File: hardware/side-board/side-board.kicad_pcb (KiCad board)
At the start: 4 copper layers, 294 parts, among them IC101 TPS62933DRLR, IC102 NUP2105LT1G, IC201 STM32C092KCT6, IC202 TCAN332DR, IC203 TPS56A37RPAR, IC204 INA181A1IDBVR, IC301 STM32C092KCT6, IC302 TCAN332DR, IC303 TPS56A37RPAR, IC304 INA181A1IDBVR, IC401 STM32C092KCT6, IC402 TCAN332DR, IC403 TPS56A37RPAR, IC404 INA181A1IDBVR, J101 Inter-board Connector, J102 Inter-board Connector, J103 XT30 VBAT, J201 Servo Connector, J202 Servo Connector, J203 Servo Connector, J204 TC2050, J205 Conn_01x06, J301 Servo Connector, J302 Servo Connector, J303 Servo Connector, J304 TC2050, J305 Conn_01x06, J401 Servo Connector, J402 Servo Connector, J403 Servo Connector, J404 TC2050, J405 Conn_01x06, Y201 Crystal_GND24, Y301 Crystal_GND24, Y401 Crystal_GND24

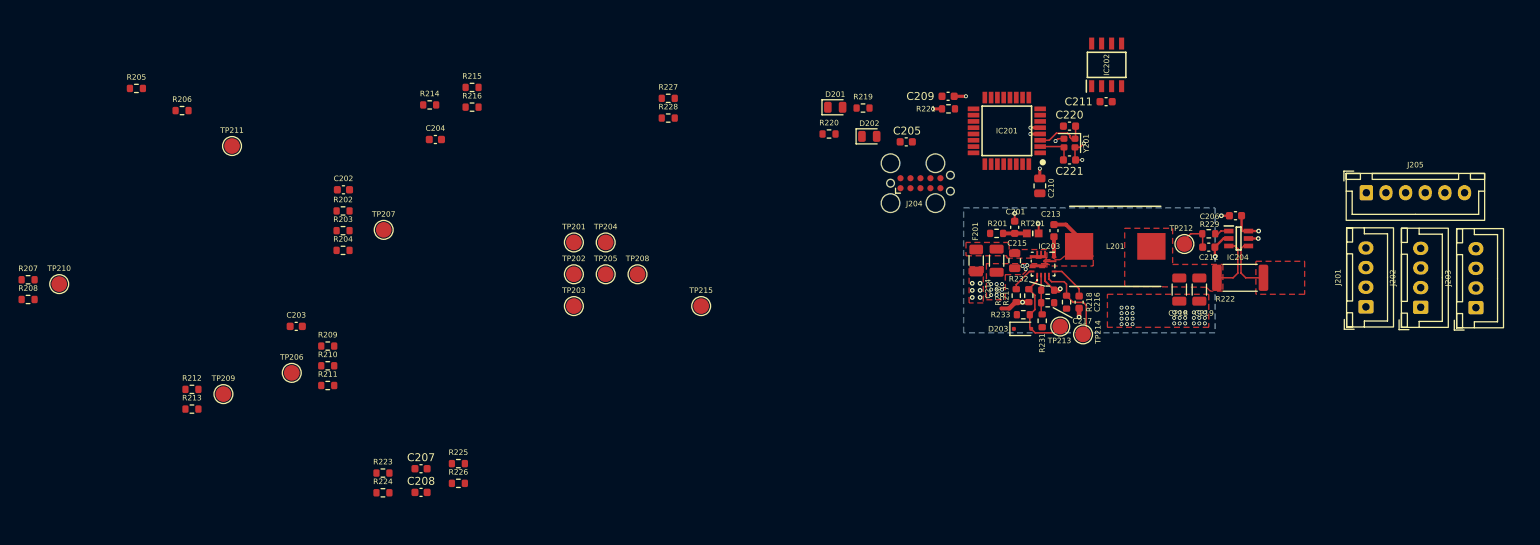
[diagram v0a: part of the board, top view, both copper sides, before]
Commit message: Updated PCB placement side-board
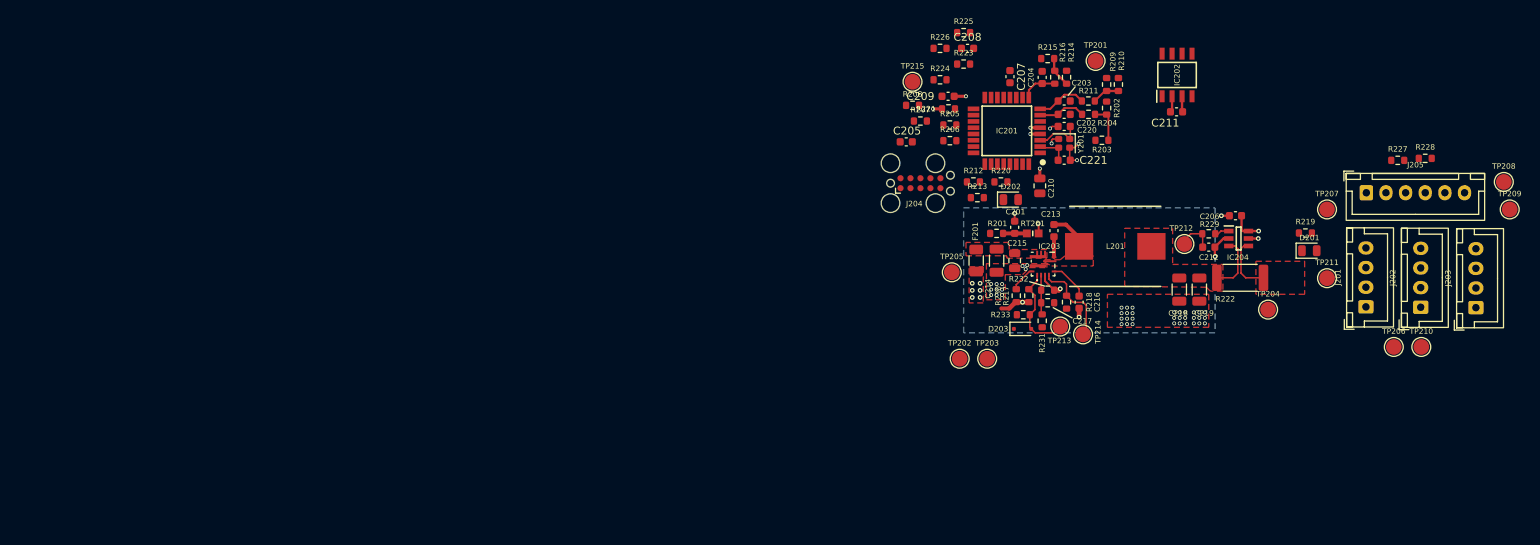
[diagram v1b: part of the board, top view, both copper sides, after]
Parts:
- moved TP210 173.5 mm to (214.8, 54.5)
- moved TP209 165.4 mm to (226.0, 37.0)
- moved TP211 140.4 mm to (202.8, 45.8)
- moved TP206 140.3 mm to (211.2, 54.5)
- moved TP207 120.1 mm to (202.8, 37.0)
- moved R207 115.3 mm to (151.0, 25.8)
- moved R208 115.2 mm to (150.0, 23.8)
- moved TP208 110.9 mm to (225.2, 33.5)
- moved R210 106.8 mm to (176.2, 21.1), turned to -90 degrees
- moved R209 104.6 mm to (174.7, 21.1), turned to -90 degrees
- moved R205 103.6 mm to (154.8, 26.2)
- moved R213 103.5 mm to (158.2, 35.5)
- moved R211 103.4 mm to (172.4, 23.2), turned to 180 degrees
- moved R212 102.9 mm to (157.8, 33.5)
- moved C203 101.9 mm to (169.3, 23.2)
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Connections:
- C216 pad 2: AGND -> /Leg_A/AGND
- C316 pad 2: AGND -> /Leg_B/AGND
- C416 pad 2: AGND -> /Leg_C/AGND
- IC203 pad 3: AGND -> /Leg_A/AGND
- IC303 pad 3: AGND -> /Leg_B/AGND
- IC403 pad 3: AGND -> /Leg_C/AGND
- NT201 pad 1: AGND -> /Leg_A/AGND
- NT301 pad 1: AGND -> /Leg_B/AGND
- NT401 pad 1: AGND -> /Leg_C/AGND
- R217 pad 1: AGND -> /Leg_A/AGND
- R230 pad 1: AGND -> /Leg_A/AGND
- R232 pad 2: AGND -> /Leg_A/AGND
- R317 pad 1: AGND -> /Leg_B/AGND
- R330 pad 1: AGND -> /Leg_B/AGND
- R332 pad 2: AGND -> /Leg_B/AGND
- R417 pad 1: AGND -> /Leg_C/AGND
- R430 pad 1: AGND -> /Leg_C/AGND
- R432 pad 2: AGND -> /Leg_C/AGND
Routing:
- net AGND: track 7.20 -> 0.00 mm, vias 3 -> 0
- net /Leg_A/AGND: track 0.00 -> 7.20 mm, vias 0 -> 3
- net /Leg_A/ADC_POT_FEMUR: track 0.00 -> 6.39 mm
- net /Leg_A/ADC_POT_COXA: track 0.00 -> 6.04 mm
- net Net-(R202-Pad2): track 0.00 -> 4.85 mm
- net /Leg_A/ADC_POT_TIBIA: track 0.00 -> 4.61 mm
- net Net-(R214-Pad2): track 0.00 -> 3.85 mm
- net Net-(R209-Pad2): track 0.00 -> 3.53 mm
- net GND: track 14.2 -> 17.6 mm, vias 51 -> 52
- net +3V3: track 9.23 -> 11.2 mm
- net /Leg_A/OSC_OUT: track 6.87 -> 6.04 mm
- net /Leg_A/OSC_IN: track 4.71 -> 4.20 mm
- added copper zone on In1.Cu, net /Leg_A/AGND
- removed copper zone on In1.Cu, net AGND

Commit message: Updated sideboard PCB
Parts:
- C101, C103, C104, C105: footprint Capacitor_SMD:C_0805_2012Metric -> Capacitor_SMD:C_0603_1608Metric
- H101, H102, H103, H104: footprint MountingHole:MountingHole_3.2mm_M3 -> MountingHole:MountingHole_3.2mm_M3_DIN965_Pad_TopBottom
- J103: footprint Connector_AMASS:AMASS_XT30PW-M_1x02_P2.50mm_Horizontal -> Connector_AMASS:AMASS_XT30U-M_1x02_P5.0mm_Vertical
- JP108: moved to B.Cu
- L101: footprint vector:INDPM116102X400N -> vector:INDPM4441X200N
- L201, L301, L401: footprint vector:INDPM116102X400N -> side-board:INDPM7973X540N
- R101, R102: footprint Resistor_SMD:R_0805_2012Metric -> Resistor_SMD:R_0603_1608Metric
- moved NT401 73.1 mm to (114.9, 181.8), turned to 180 degrees
- moved JP108 57.7 mm to (30.6, 119.7)
- moved J303 57.4 mm to (206.6, 122.7), turned to 90 degrees
- moved J403 57.4 mm to (174.8, 181.7), turned to 90 degrees
- moved NT301 57.3 mm to (146.7, 122.8), turned to 180 degrees
- moved C308 57.1 mm to (141.9, 89.7)
- moved C408 57.1 mm to (110.1, 148.7)
- moved C309 56.9 mm to (139.4, 95.8)
- moved C409 56.9 mm to (107.6, 154.8)
- moved J301 54.0 mm to (192.6, 122.5), turned to 90 degrees
- moved J401 54.0 mm to (160.8, 181.6), turned to 90 degrees
- moved J302 53.1 mm to (199.5, 122.6), turned to 90 degrees
- moved J402 53.1 mm to (167.8, 181.6), turned to 90 degrees
- moved C405 52.4 mm to (102.3, 160.6), turned to 180 degrees
- moved C305 52.4 mm to (134.1, 101.5), turned to 180 degrees
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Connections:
- net Net-(IC101-SW) renamed /SW
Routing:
- net GND: track 17.6 -> 52.9 mm, vias 52 -> 156
- net +3V3: track 11.2 -> 33.7 mm, vias 5 -> 15
- net /Leg_B/BUCK_EN: track 0.00 -> 12.2 mm
- net /Leg_C/BUCK_EN: track 0.00 -> 12.2 mm
- net /Leg_C/BUCK_PG: track 0.00 -> 11.4 mm
- net /Leg_B/BUCK_PG: track 0.00 -> 11.4 mm
- net /Leg_B/6V0_BUCK: track 0.00 -> 7.31 mm
- net /Leg_C/6V0_BUCK: track 0.00 -> 7.31 mm
- net /Leg_B/6V0: track 0.00 -> 7.31 mm
- net /Leg_C/6V0: track 0.00 -> 7.31 mm
- net /Leg_C/AGND: track 0.00 -> 7.20 mm, vias 0 -> 3
- net /Leg_B/AGND: track 0.00 -> 7.20 mm, vias 0 -> 3
- net /Leg_B/ADC_POT_FEMUR: track 0.00 -> 6.39 mm
- net /Leg_C/ADC_POT_FEMUR: track 0.00 -> 6.39 mm
- net /Leg_B/ADC_POT_COXA: track 0.00 -> 6.04 mm
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- added copper zone on F.Cu, net /Leg_B/6V0
- added copper zone on F.Cu, net /Leg_B/6V0_BUCK
- added copper zone on In1.Cu, net /Leg_B/AGND
- added copper zone on F.Cu, net /Leg_B/SW
- added copper zone on F.Cu, net /Leg_B/VBAT_F
- added copper zone on F.Cu, net /Leg_C/6V0
- added copper zone on F.Cu, net /Leg_C/6V0_BUCK
- added copper zone on In1.Cu, net /Leg_C/AGND
- added copper zone on F.Cu, net /Leg_C/SW
- added copper zone on F.Cu, net /Leg_C/VBAT_F
- added copper zone on F.Cu, net /SW

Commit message: Updated PCB placement sideboard
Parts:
- JP107: value Jumper_Open -> SIDE_BIT
- R203, R210, R215: moved to B.Cu
- moved C106 70.5 mm to (89.4, 89.5), turned to 0 degrees
- moved J101 66.6 mm to (85.0, 140.0)
- moved D101 60.7 mm to (88.7, 73.4)
- moved TP101 54.3 mm to (69.0, 135.5)
- moved TP102 51.7 mm to (75.8, 135.4)
- moved J102 47.9 mm to (71.5, 140.0)
- moved TP105 43.3 mm to (101.0, 82.2)
- moved IC102 36.0 mm to (72.5, 135.2), turned to 90 degrees
- moved TP104 35.4 mm to (42.8, 124.5), turned to -90 degrees
- moved C205 24.8 mm to (173.9, 26.4)
- moved D102 23.4 mm to (33.8, 116.6), turned to 90 degrees
- moved R104 23.1 mm to (69.1, 133.2), turned to 180 degrees
- moved TP103 22.4 mm to (80.4, 79.2)
- moved J103 21.1 mm to (86.3, 81.4)
- moved JP107 19.6 mm to (56.9, 104.4)
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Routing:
- net /Leg_A/ADC_POT_FEMUR: track 6.39 -> 0.00 mm
- net /Leg_A/ADC_POT_COXA: track 6.04 -> 0.00 mm
- net Net-(R202-Pad2): track 4.85 -> 0.00 mm
- net /CAN_L: track 0.00 -> 4.08 mm
- net Net-(R214-Pad2): track 3.85 -> 0.00 mm
- net /CAN_H: track 0.00 -> 3.80 mm
- net Net-(R209-Pad2): track 3.53 -> 0.00 mm
- net GND: track 52.9 -> 56.3 mm
- net /VBAT: track 0.00 -> 3.01 mm
- net /Leg_A/ADC_POT_TIBIA: track 4.61 -> 1.69 mm
- net /Leg_A/6V0_ADC: track 0.00 -> 2.66 mm
- net +3V3: track 33.7 -> 36.2 mm, vias 15 -> 13
- net /Leg_A/VBAT_ADC: track 0.00 -> 2.43 mm
- net /SW: track 4.00 -> 3.44 mm
- added copper zone on F.Cu, net +3V3

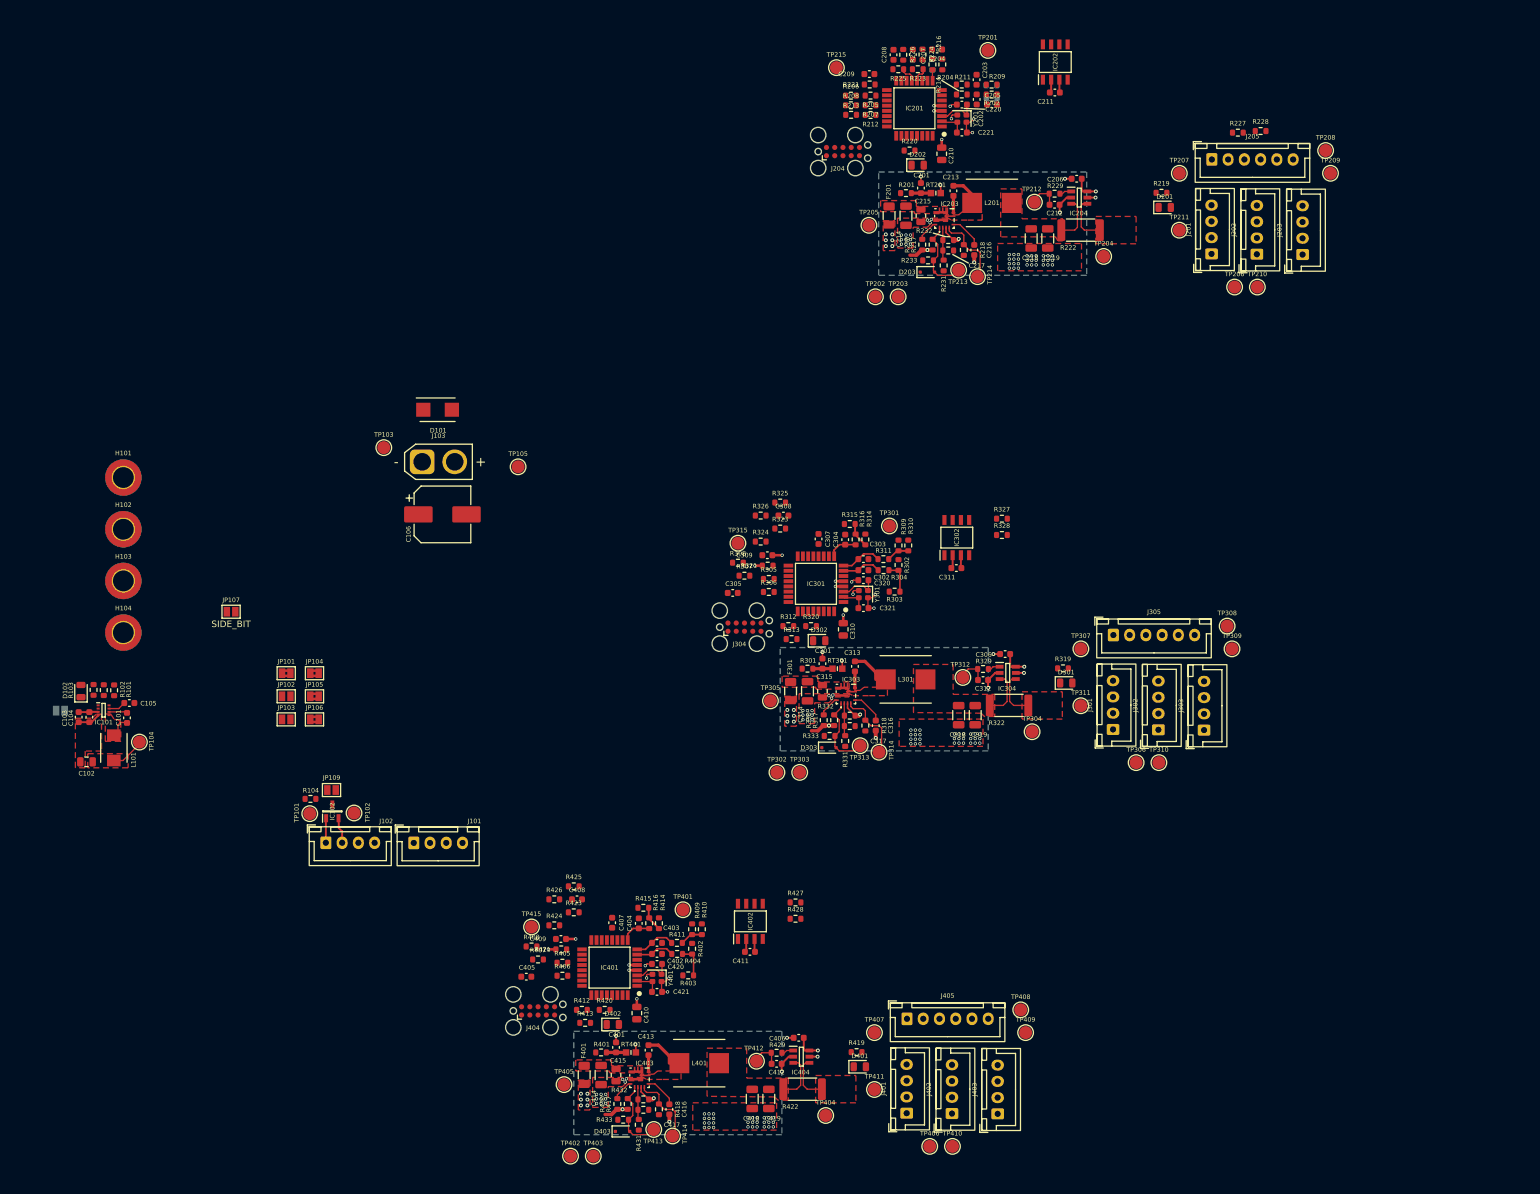
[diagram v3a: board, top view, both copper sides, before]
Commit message: Compacted side board pcb
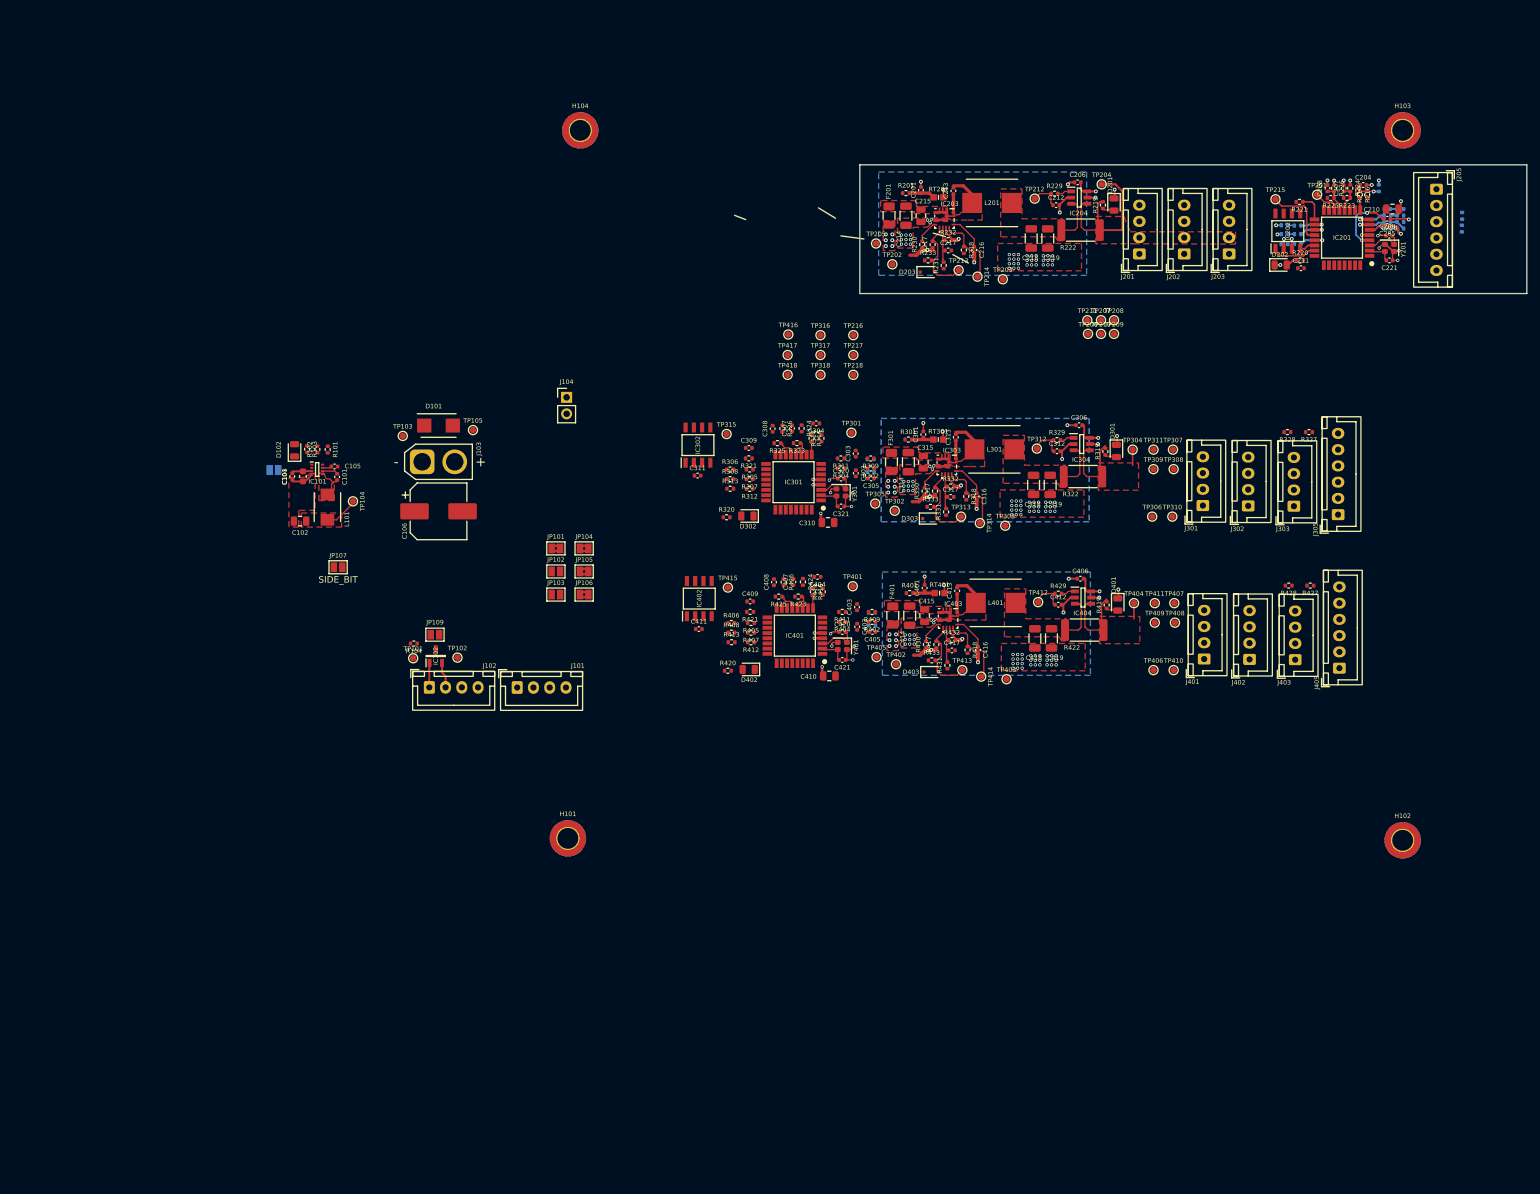
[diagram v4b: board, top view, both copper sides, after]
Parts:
- removed J204, J304, J404: TC2050, Connector:Tag-Connect_TC2050-IDC-FP_2x05_P1.27mm_Vertical
- added J104: SWD PWR, Connector_PinHeader_2.54mm:PinHeader_1x02_P2.54mm_Vertical, F.Cu at (108.5, 71.5)
- added TP216: SWDIO, TestPoint:TestPoint_Pad_D1.0mm, F.Cu at (152.6, 61.9)
- added TP217: SWCLK, TestPoint:TestPoint_Pad_D1.0mm, F.Cu at (152.6, 65.0)
- added TP218: NRST, TestPoint:TestPoint_Pad_D1.0mm, F.Cu at (152.6, 68.0)
- added TP316: SWDIO, TestPoint:TestPoint_Pad_D1.0mm, F.Cu at (147.6, 61.9)
- added TP317: SWCLK, TestPoint:TestPoint_Pad_D1.0mm, F.Cu at (147.6, 65.0)
- added TP318: NRST, TestPoint:TestPoint_Pad_D1.0mm, F.Cu at (147.6, 68.0)
- added TP416: SWDIO, TestPoint:TestPoint_Pad_D1.0mm, F.Cu at (142.6, 61.8)
- added TP417: SWCLK, TestPoint:TestPoint_Pad_D1.0mm, F.Cu at (142.5, 65.0)
- added TP418: NRST, TestPoint:TestPoint_Pad_D1.0mm, F.Cu at (142.5, 68.0)
- C101, C105, C201, C204, C205, C206, C207, C208, C209, C211, C212, C213, C216, C220, C221, C301, C302, C303, C304, C305, C306, C307, C308, C309, C311, C312, C313, C316, C320, C321, C401, C402, C403, C404, C405, C406, C407, C408, C409, C411, C412, C413, C416, C420, C421: footprint Capacitor_SMD:C_0603_1608Metric -> Capacitor_SMD:C_0402_1005Metric
- C103: value 100n -> 100n 50V; footprint Capacitor_SMD:C_0603_1608Metric -> Capacitor_SMD:C_0402_1005Metric
- C202, C203: footprint Capacitor_SMD:C_0603_1608Metric -> Capacitor_SMD:C_0402_1005Metric; moved to B.Cu
- C217, C317, C417: footprint Resistor_SMD:R_0603_1608Metric -> Capacitor_SMD:C_0402_1005Metric
- R101, R102, R103, R104, R201, R203, R210, R214, R215, R216, R217, R218, R219, R220, R221, R223, R224, R225, R226, R229, R230, R231, R232, R233, R301, R302, R304, R305, R306, R307, R308, R309, R311, R312, R313, R314, R316, R317, R318, R319, R320, R321, R323, R324, R325, R326, R327, R328, R329, R330, R331, R332, R333, R401, R402, R404, R405, R406, R407, R408, R409, R411, R412, R413, R414, R416, R417, R418, R419, R420, R421, R423, R424, R425, R426, R427, R428, R429, R430, R431, R432, R433: footprint Resistor_SMD:R_0603_1608Metric -> Resistor_SMD:R_0402_1005Metric
- R202, R204, R205, R206, R207, R208, R209, R211, R212, R213, R227, R228, R303, R310, R315, R403, R410, R415: footprint Resistor_SMD:R_0603_1608Metric -> Resistor_SMD:R_0402_1005Metric; moved to B.Cu
- TP101, TP102, TP103, TP104, TP105, TP201, TP202, TP203, TP204, TP205, TP206, TP207, TP208, TP209, TP210, TP211, TP212, TP213, TP214, TP215, TP301, TP302, TP303, TP304, TP305, TP306, TP307, TP308, TP309, TP310, TP311, TP312, TP313, TP314, TP315, TP401, TP402, TP403, TP404, TP405, TP406, TP407, TP408, TP409, TP410, TP411, TP412, TP413, TP414, TP415: footprint TestPoint:TestPoint_Pad_D2.0mm -> TestPoint:TestPoint_Pad_D1.0mm
- moved H103 208.6 mm to (237.1, 30.4)
- moved H102 202.5 mm to (237.1, 139.6)
- moved H104 104.4 mm to (110.6, 30.4)
- moved TP403 97.1 mm to (176.2, 114.8)
- moved R427 93.0 mm to (222.9, 100.4), turned to 180 degrees
- moved TP404 92.0 mm to (195.8, 103.1)
- moved R428 91.6 mm to (219.6, 100.4), turned to 180 degrees
- moved TP402 90.7 mm to (159.2, 112.5)
- moved H101 88.1 mm to (108.7, 139.3)
- moved TP411 86.3 mm to (199.0, 103.1)
- moved J405 85.6 mm to (227.4, 113.1), turned to 90 degrees
- moved TP413 85.1 mm to (169.4, 113.4)
- moved C401 85.1 mm to (163.6, 100.8)
- moved C414 85.1 mm to (161.3, 105.0)
- moved C415 85.1 mm to (163.6, 105.0)
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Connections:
- R204 pad 1: Net-(R202-Pad2) -> /Leg_A/ADC_POT_COXA
- R204 pad 2: /Leg_A/ADC_POT_COXA -> Net-(R202-Pad2)
- R304 pad 1: Net-(R302-Pad2) -> /Leg_B/ADC_POT_COXA
- R304 pad 2: /Leg_B/ADC_POT_COXA -> Net-(R302-Pad2)
- R404 pad 1: Net-(R402-Pad2) -> /Leg_C/ADC_POT_COXA
- R404 pad 2: /Leg_C/ADC_POT_COXA -> Net-(R402-Pad2)
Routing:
- net GND: track 56.3 -> 75.2 mm, vias 156 -> 172
- net /Leg_A/6V0: track 7.42 -> 25.5 mm
- net /Leg_A/PC6: track 0.00 -> 10.6 mm
- net /Leg_C/6V0: track 7.31 -> 15.0 mm
- net /Leg_B/6V0: track 7.31 -> 15.0 mm
- net /Leg_A/CAN_TX: track 0.00 -> 7.06 mm
- net /Leg_A/ADC_POT_FEMUR: track 0.00 -> 6.43 mm, vias 0 -> 1
- net /Leg_B/ADC_POT_FEMUR: track 6.39 -> 0.00 mm
- net /Leg_C/ADC_POT_FEMUR: track 6.39 -> 0.00 mm
- net /Leg_A/ADC_POT_COXA: track 0.00 -> 6.34 mm, vias 0 -> 1
- net /Leg_B/ADC_POT_COXA: track 6.04 -> 0.00 mm
- net /Leg_C/ADC_POT_COXA: track 6.04 -> 0.00 mm
- net Net-(R302-Pad2): track 4.85 -> 0.00 mm
- net Net-(R402-Pad2): track 4.85 -> 0.00 mm
- net /Leg_A/TIM_PWM_TIBIA: track 0.00 -> 4.72 mm, vias 0 -> 1
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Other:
- board outline added: 102.6 x 19.8 mm
